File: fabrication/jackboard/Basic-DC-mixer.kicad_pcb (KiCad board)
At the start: 2 copper layers, 40 x 110 mm, 33 parts, among them J1 In, J2 Power Input, J3 In, J4 InvOut, J5 Out, J6 In, J7 In, SW1 Mute, SW2 Mute, SW3 Mute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

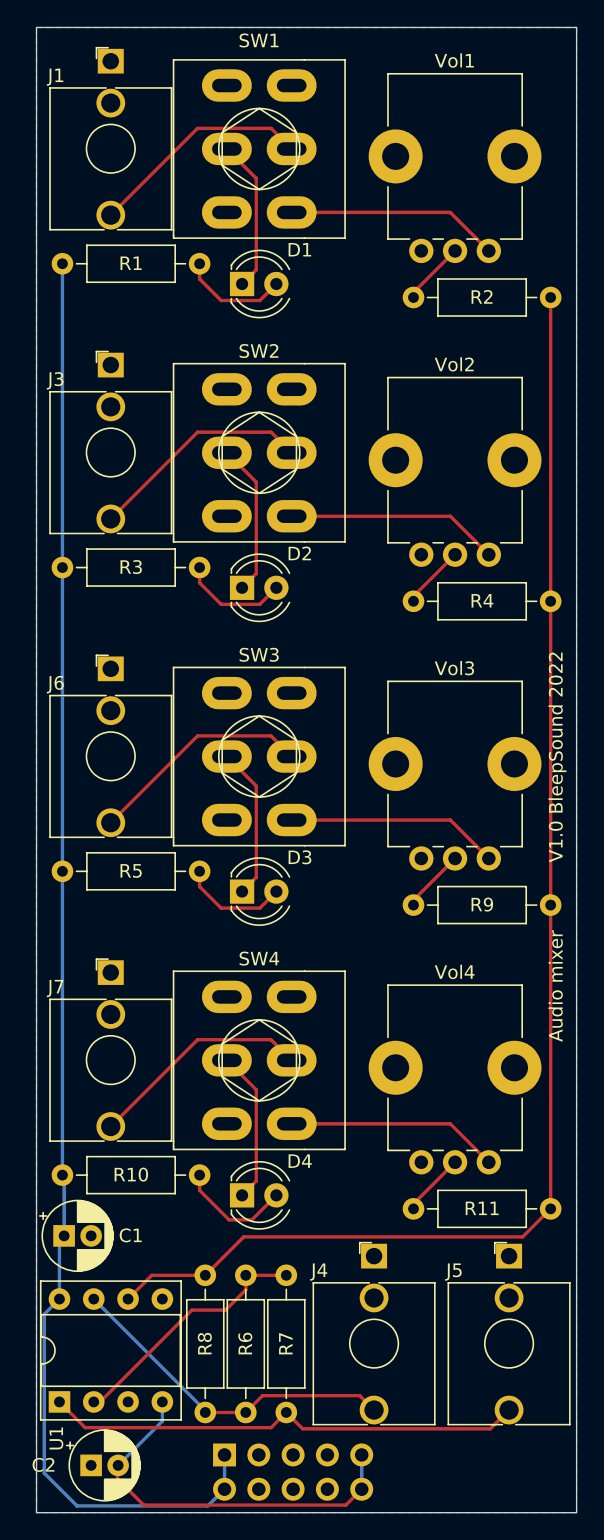
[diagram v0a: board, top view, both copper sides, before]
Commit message: update silkscreen and hole diameter
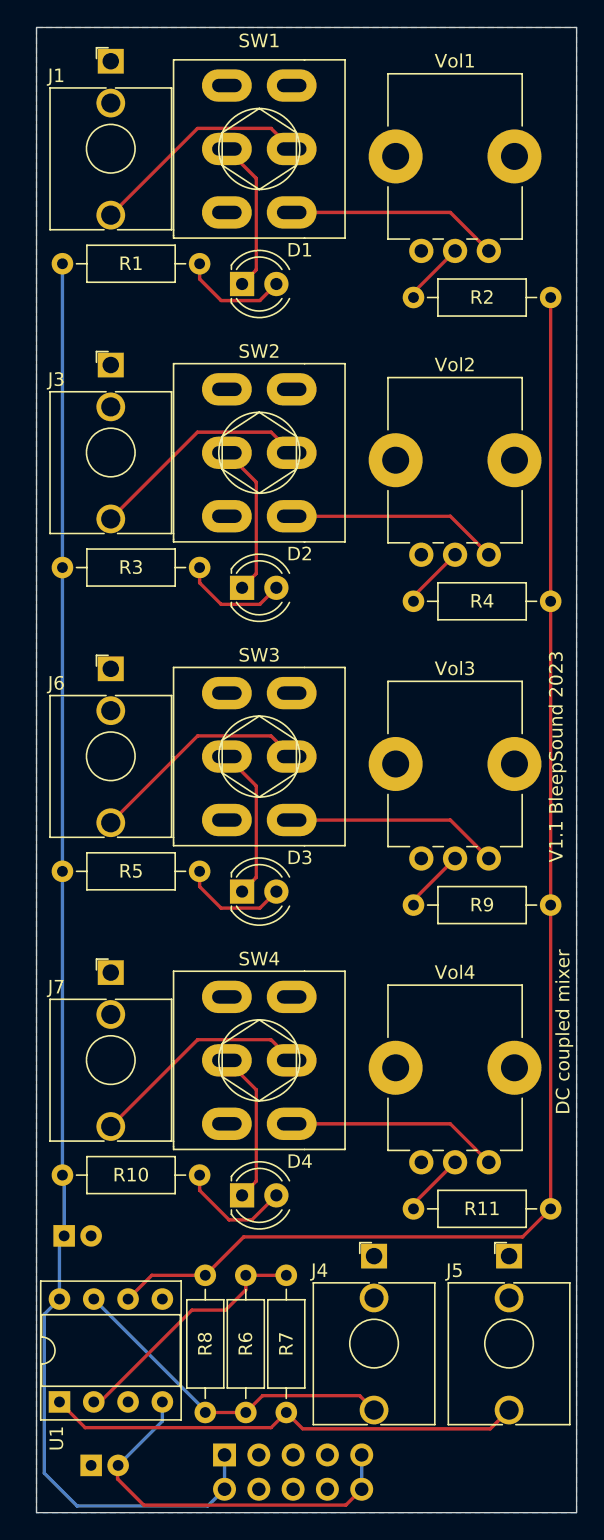
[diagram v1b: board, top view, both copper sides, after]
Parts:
- C1, C2: moved to B.Cu
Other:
- board text added: "DC coupled mixer"
- board text added: "V1.1 BleepSound 2023"
- board text removed: "Audio mixer"
- board text removed: "V1.0 BleepSound 2022"

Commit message: update mixer to v1.2, update repo organization
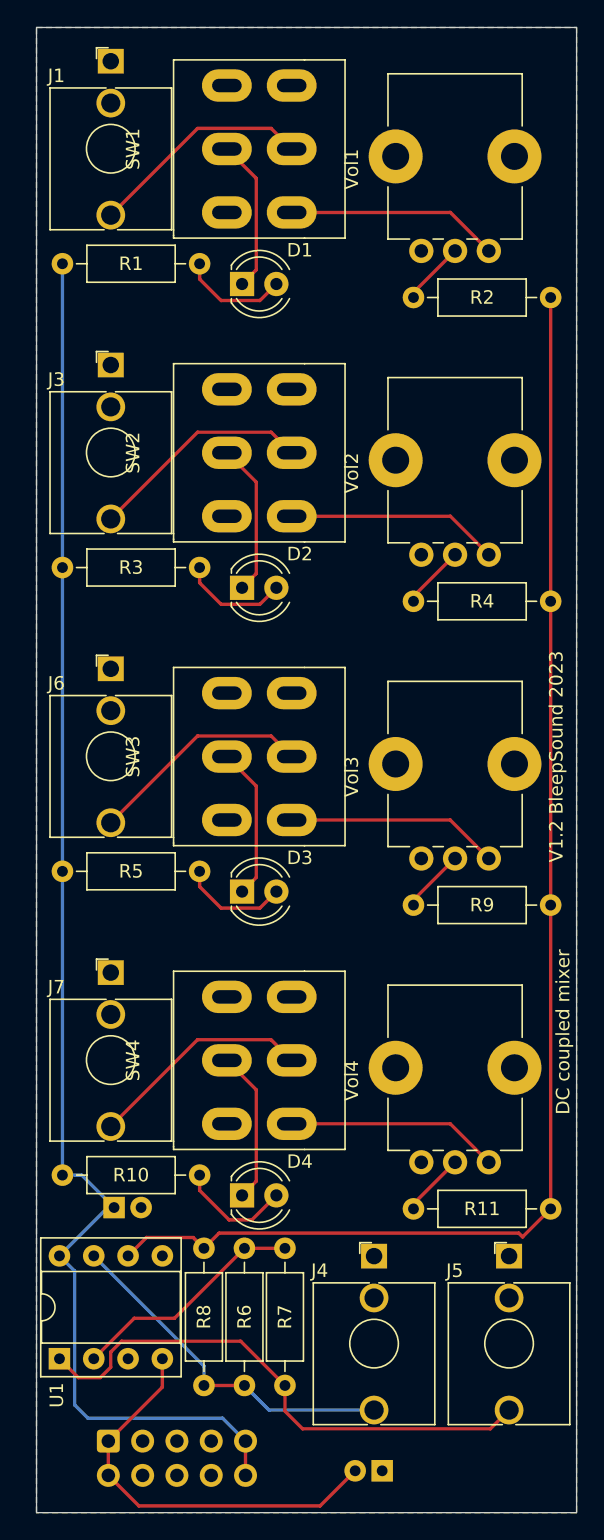
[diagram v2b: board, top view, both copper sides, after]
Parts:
- J1, J3, J4, J5, J6, J7: footprint Synth:Thonkiconn -> Kicad-perso:Thonkiconn
- J2: footprint Connector_PinHeader_2.54mm:PinHeader_2x05_P2.54mm_Vertical -> Connector_IDC:IDC-Header_2x05_P2.54mm_Vertical
- SW1, SW2, SW3, SW4: footprint Synth:SW_DPDT_Toggle -> Kicad-perso:SW_DPDT_Toggle
- Vol1, Vol2, Vol3, Vol4: footprint Synth:Pot-bourns-alpha -> Kicad-perso:Pot-bourns-alpha
- moved C2 21.6 mm to (55.6, 137.9), turned to 180 degrees
- moved J2 8.67 mm to (35.3, 135.7)
- moved C1 4.25 mm to (35.7, 118.4)
- moved U1 3.20 mm to (31.7, 129.6)
- moved R6 2.00 mm to (45.4, 121.4)
- moved R7 2.00 mm to (48.4, 131.6)
- moved R8 2.00 mm to (42.4, 131.6)
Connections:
- J2 pad 1: +12V -> -12V
- J2 pad 10: -12V -> +12V
- J2 pad 2: +12V -> -12V
- J2 pad 9: -12V -> +12V
- Vol1 pad 1: Net-(SW1-C-Pad6) -> GND
- Vol1 pad 3: GND -> Net-(SW1-C-Pad6)
- Vol2 pad 1: Net-(SW2-C-Pad6) -> GND
- Vol2 pad 3: GND -> Net-(SW2-C-Pad6)
- Vol3 pad 1: Net-(SW3-C-Pad6) -> GND
- Vol3 pad 3: GND -> Net-(SW3-C-Pad6)
- Vol4 pad 1: Net-(SW4-C-Pad6) -> GND
- Vol4 pad 3: GND -> Net-(SW4-C-Pad6)
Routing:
- net Net-(J5-PadT): track 35.6 -> 40.0 mm
- net +12V: track 107.6 -> 105.8 mm
- net -12V: track 29.0 -> 30.6 mm
- net Net-(U1A--): track 18.8 -> 17.5 mm
- net Net-(J4-PadT): track 25.3 -> 26.3 mm
- added copper zone on F.Cu, net GND
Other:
- board text added: "V1.2 BleepSound 2023"
- board text removed: "V1.1 BleepSound 2023"
